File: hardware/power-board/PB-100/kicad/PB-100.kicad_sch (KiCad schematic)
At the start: 0 parts

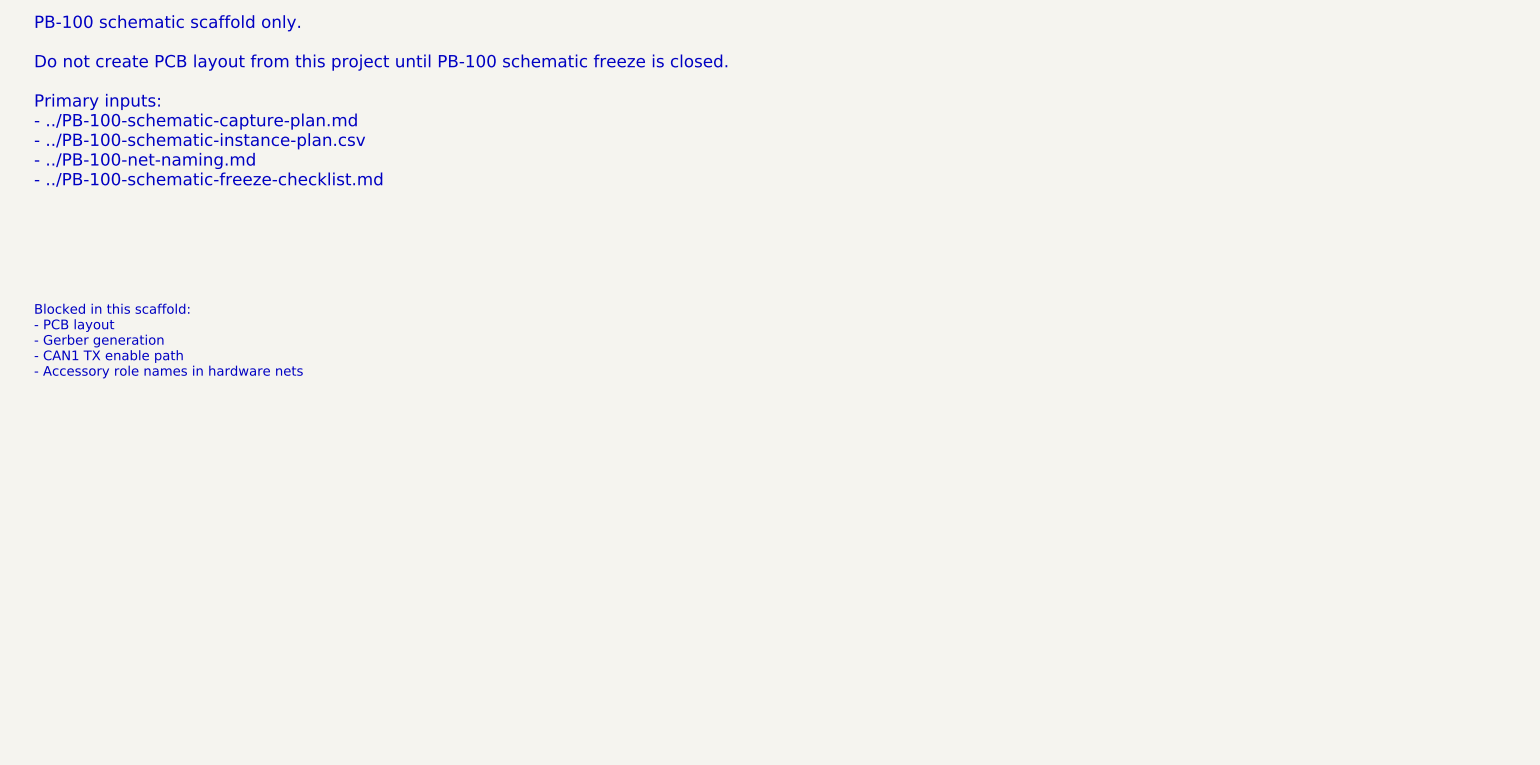
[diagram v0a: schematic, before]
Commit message: hardware: link pb100 kicad child sheets
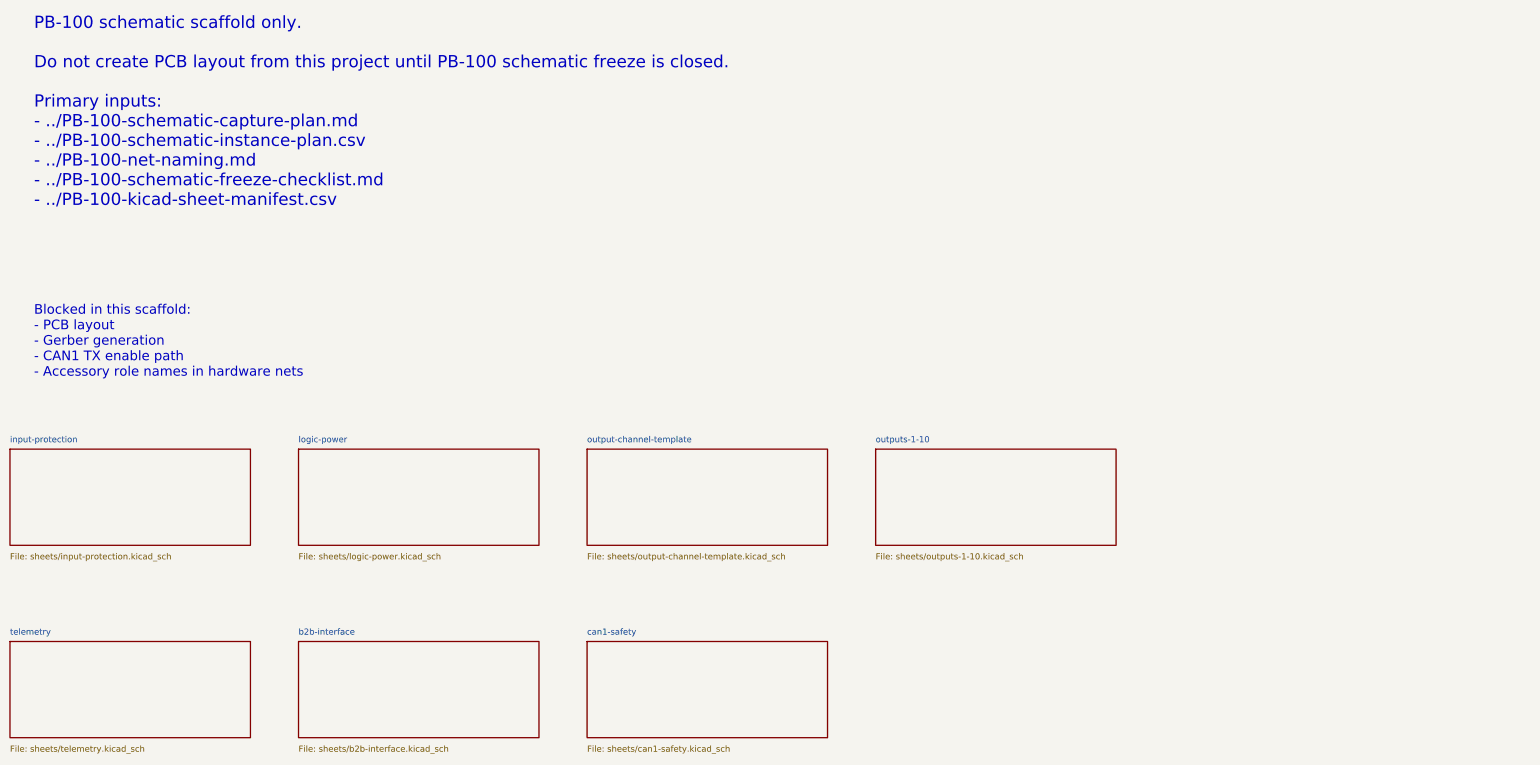
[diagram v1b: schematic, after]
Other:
- added sheet b2b-interface (sheets/b2b-interface.kicad_sch)
- added sheet can1-safety (sheets/can1-safety.kicad_sch)
- added sheet input-protection (sheets/input-protection.kicad_sch)
- added sheet logic-power (sheets/logic-power.kicad_sch)
- added sheet output-channel-template (sheets/output-channel-template.kicad_sch)
- added sheet outputs-1-10 (sheets/outputs-1-10.kicad_sch)
- added sheet telemetry (sheets/telemetry.kicad_sch)
- note added: "PB-100 schematic scaffold only. Do not create PCB layout from this project until PB-100 schematic freeze is closed. Primary inputs: - ../PB-100-schematic-capture-plan.md - ../PB-100-schematic-instance-plan.csv - ../PB-100-net-naming.md - ../PB-100-schematic-freeze-checklist.md - ../PB-100-kicad-sheet-manifest.csv"
- note removed: "PB-100 schematic scaffold only. Do not create PCB layout from this project until PB-100 schematic freeze is closed. Primary inputs: - ../PB-100-schematic-capture-plan.md - ../PB-100-schematic-instance-plan.csv - ../PB-100-net-naming.md - ../PB-100-schematic-freeze-checklist.md"
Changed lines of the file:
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@@
     (comment 4 "Outputs are generic OUT1..OUT10; roles are configuration-only.")
   )
-  (text "PB-100 schematic scaffold only.\n\nDo not create PCB layout from this project until PB-100 schematic freeze is closed.\n\nPrimary inputs:\n- ../PB-100-schematic-capture-plan.md\n- ../PB-100-schematic-instance-plan.csv\n- ../PB-100-net-naming.md\n- ../PB-100-schematic-freeze-checklist.md"
+  (text "PB-100 schematic scaffold only.\n\nDo not create PCB layout from this project until PB-100 schematic freeze is closed.\n\nPrimary inputs:\n- ../PB-100-schematic-capture-plan.md\n- ../PB-100-schematic-instance-plan.csv\n- ../PB-100-net-naming.md\n- ../PB-100-schematic-freeze-checklist.md\n- ../PB-100-kicad-sheet-manifest.csv"
     (at 30 35 0)
     (effects
@@
     )
   )
+  (sheet
+    (at 25 125)
+    (size 50 20)
+    (stroke
+      (width 0.1524)
+      (type solid)
+    )
+    (fill
+      (color 0 0 0 0.0000)
+    )
+    (property "Sheetname" "input-protection"
+      (at 25 123.73 0)
+      (effects
+        (font
+          (size 1.27 1.27)
+        )
+        (justify left bottom)
+      )
+    )
+    (property "Sheetfile" "sheets/input-protection.kicad_sch"
+      (at 25 146.59 0)
+      (effects
+        (font
+          (size 1.27 1.27)
+        )
+        (justify left top)
+      )
+    )
+  )
+  (sheet
+    (at 85 125)
+    (size 50 20)
+    (stroke
+      (width 0.1524)
+      (type solid)
+    )
+    (fill
+      (color 0 0 0 0.0000)
+    )
+    (property "Sheetname" "logic-power"
+      (at 85 123.73 0)
+      (effects
+        (font
+          (size 1.27 1.27)
+        )
+        (justify left bottom)
+      )
+    )
+    (property "Sheetfile" "sheets/logic-power.kicad_sch"
+      (at 85 146.59 0)
+      (effects
+        (font
+          (size 1.27 1.27)
+        )
+        (justify left top)
+      )
+    )
+  )
+  (sheet
+    (at 145 125)
+    (size 50 20)
+    (stroke
+      (width 0.1524)
+      (type solid)
+    )
+    (fill
+      (color 0 0 0 0.0000)
+    )
+    (property "Sheetname" "output-channel-template"
+      (at 145 123.73 0)
+      (effects
+        (font
+          (size 1.27 1.27)
+        )
+        (justify left bottom)
+      )
+    )
+    (property "Sheetfile" "sheets/output-channel-template.kicad_sch"
+      (at 145 146.59 0)
+      (effects
+        (font
+          (size 1.27 1.27)
+        )
+        (justify left top)
+      )
+    )
+  )
+  (sheet
+    (at 205 125)
+    (size 50 20)
+    (stroke
+      (width 0.1524)
+      (type solid)
+    )
+    (fill
+      (color 0 0 0 0.0000)
+    )
+    (property "Sheetname" "outputs-1-10"
+      (at 205 123.73 0)
+      (effects
+        (font
+          (size 1.27 1.27)
+        )
+        (justify left bottom)
+      )
+    )
+    (property "Sheetfile" "sheets/outputs-1-10.kicad_sch"
+      (at 205 146.59 0)
+      (effects
+        (font
+          (size 1.27 1.27)
+        )
+        (justify left top)
+      )
+    )
+  )
+  (sheet
+    (at 25 165)
+    (size 50 20)
+    (stroke
+      (width 0.1524)
+      (type solid)
+    )
+    (fill
+      (color 0 0 0 0.0000)
+    )
+    (property "Sheetname" "telemetry"
+      (at 25 163.73 0)
+      (effects
+        (font
+          (size 1.27 1.27)
+        )
+        (justify left bottom)
+      )
+    )
+    (property "Sheetfile" "sheets/telemetry.kicad_sch"
+      (at 25 186.59 0)
+      (effects
+        (font
+          (size 1.27 1.27)
+        )
+        (justify left top)
+      )
+    )
+  )
+  (sheet
+    (at 85 165)
+    (size 50 20)
+    (stroke
+      (width 0.1524)
+      (type solid)
+    )
+    (fill
+      (color 0 0 0 0.0000)
+    )
+    (property "Sheetname" "b2b-interface"
+      (at 85 163.73 0)
+      (effects
+        (font
+          (size 1.27 1.27)
+        )
+        (justify left bottom)
+      )
+    )
+    (property "Sheetfile" "sheets/b2b-interface.kicad_sch"
+      (at 85 186.59 0)
+      (effects
+        (font
+          (size 1.27 1.27)
+        )
+        (justify left top)
+      )
+    )
+  )
+  (sheet
+    (at 145 165)
+    (size 50 20)
+    (stroke
+      (width 0.1524)
+      (type solid)
+    )
+    (fill
+      (color 0 0 0 0.0000)
+    )
+    (property "Sheetname" "can1-safety"
+      (at 145 163.73 0)
+      (effects
+        (font
+          (size 1.27 1.27)
+        )
+        (justify left bottom)
+      )
+    )
+    (property "Sheetfile" "sheets/can1-safety.kicad_sch"
+      (at 145 186.59 0)
+      (effects
+        (font
+          (size 1.27 1.27)
+        )
+        (justify left top)
+      )
+    )
+  )

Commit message: hardware: correct fog entry and EVT layout gates
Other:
- added sheet fog-switch-entry (sheets/fog-switch-entry.kicad_sch)
- note added: "Current boundary: - EVT layout authorized - Gerber and ordering blocked - CAN1 TX enable path blocked - Accessory role names forbidden in hardware nets"
- note added: "PB-100 Rev.1 EVT schematic capture. Placement and routing are authorized under ADR-0020/ADR-0021. Manufacturing output remains blocked until EVT-FAB-AUTHORIZED. Primary inputs: - ../PB-100-schematic-capture-plan.md - ../PB-100-schematic-instance-plan.csv - ../PB-100-net-naming.md - ../PB-100-schematic-freeze-checklist.md - ../PB-100-kicad-sheet-manifest.csv"
- note removed: "Blocked in this scaffold: - PCB layout - Gerber generation - CAN1 TX enable path - Accessory role names in hardware nets"
- note removed: "PB-100 schematic scaffold only. Do not create PCB layout from this project until PB-100 schematic freeze is closed. Primary inputs: - ../PB-100-schematic-capture-plan.md - ../PB-100-schematic-instance-plan.csv - ../PB-100-net-naming.md - ../PB-100-schematic-freeze-checklist.md - ../PB-100-kicad-sheet-manifest.csv"
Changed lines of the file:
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@@
     (title "PB-100 Power Board")
     (date "2026-06-30")
-    (rev "schematic-scaffold")
+    (rev "rev1-evt-layout")
     (company "SVC Platform")
     (comment 9 "Work queue: CAP-TOP. Top-level scaffold follows PB-100-schematic-capture-work-queue.csv.")
-    (comment 1 "Schematic scaffold only. PCB layout is blocked until schematic freeze.")
+    (comment 1 "EVT layout is authorized; fabrication remains blocked pending routed review.")
     (comment 2 "Follow ../PB-100-schematic-capture-plan.md and ../PB-100-net-naming.md.")
     (comment 3 "CAN1 TX remains DNP/open and hardware-disabled by default.")
     (comment 4 "Outputs are generic OUT1..OUT10; roles are configuration-only.")
   )
-  (text "PB-100 schematic scaffold only.\n\nDo not create PCB layout from this project until PB-100 schematic freeze is closed.\n\nPrimary inputs:\n- ../PB-100-schematic-capture-plan.md\n- ../PB-100-schematic-instance-plan.csv\n- ../PB-100-net-naming.md\n- ../PB-100-schematic-freeze-checklist.md\n- ../PB-100-kicad-sheet-manifest.csv"
+  (text "PB-100 Rev.1 EVT schematic capture.\n\nPlacement and routing are authorized under ADR-0020/ADR-0021. Manufacturing output remains blocked until EVT-FAB-AUTHORIZED.\n\nPrimary inputs:\n- ../PB-100-schematic-capture-plan.md\n- ../PB-100-schematic-instance-plan.csv\n- ../PB-100-net-naming.md\n- ../PB-100-schematic-freeze-checklist.md\n- ../PB-100-kicad-sheet-manifest.csv"
     (at 30 35 0)
     (effects
@@
     )
   )
-  (text "Blocked in this scaffold:\n- PCB layout\n- Gerber generation\n- CAN1 TX enable path\n- Accessory role names in hardware nets"
+  (text "Current boundary:\n- EVT layout authorized\n- Gerber and ordering blocked\n- CAN1 TX enable path blocked\n- Accessory role names forbidden in hardware nets"
     (at 30 95 0)
     (effects
@@
       (effects
         (font
+          (size 1.27 1.27)
+        )
+        (justify left top)
+      )
+    )
+  )
+  (sheet
+    (at 205 165)
+    (size 50 20)
+    (stroke
+      (width 0.1524)
+      (type solid)
+    )
+    (fill
+      (color 0 0 0 0.0000)
+    )
+    (property "Sheetname" "fog-switch-entry"
+      (at 205 163.73 0)
+      (effects
+        (font
+          (size 1.27 1.27)
+        )
+        (justify left bottom)
+      )
+    )
+    (property "Sheetfile" "sheets/fog-switch-entry.kicad_sch"
+      (at 205 186.59 0)
+      (effects
+        (font
